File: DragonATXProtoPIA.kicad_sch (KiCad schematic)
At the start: 79 parts, among them IC1 MC6821, IC10 MT8816, IC11 74LS138, IC12 W65C51, IC13 MAX232, IC14 M48Tx2, IC15 74LS21, IC2 MC6821, IC3 74LS138, IC4 4050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

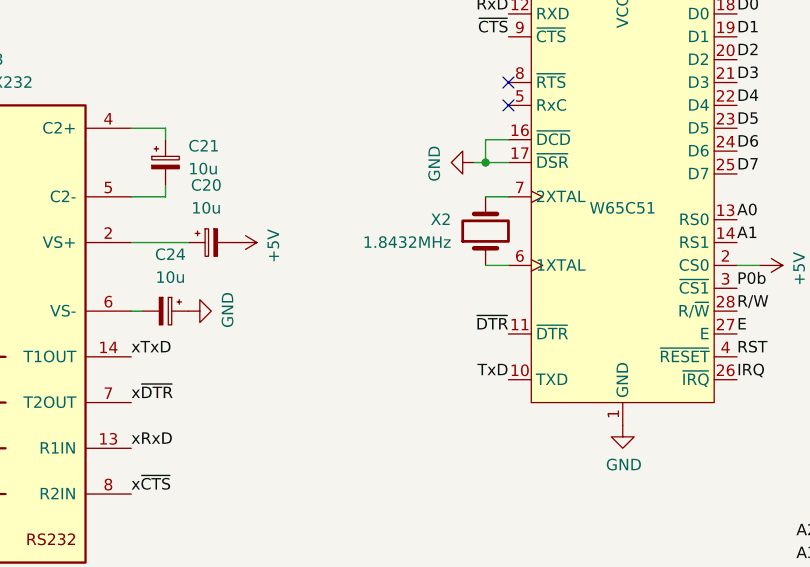
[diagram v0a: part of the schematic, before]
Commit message: Rectify slot edge and vertical dimensions
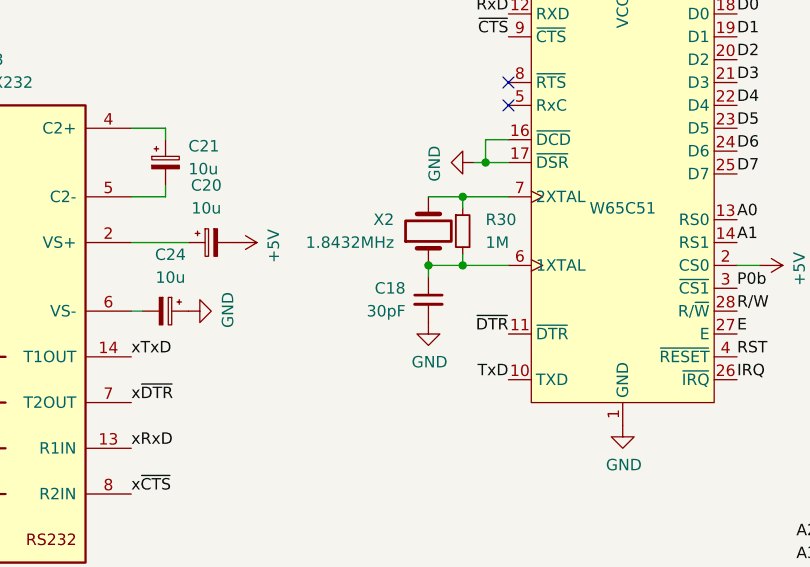
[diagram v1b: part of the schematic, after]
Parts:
- added C18: 30pF, Capacitor_THT:C_Disc_D4.3mm_W1.9mm_P5.00mm, symbol Device:C_Small
- added R30: 1M, Resistor_THT:R_Axial_DIN0204_L3.6mm_D1.6mm_P5.08mm_Horizontal, symbol Device:R_Small
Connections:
- net GND: now also C18.2
- net at IC12.6 (1XTAL), X2.1: now also C18.1, R30.2
- net at IC12.7 (2XTAL), X2.2: now also R30.1
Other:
- moved on the sheet: X2

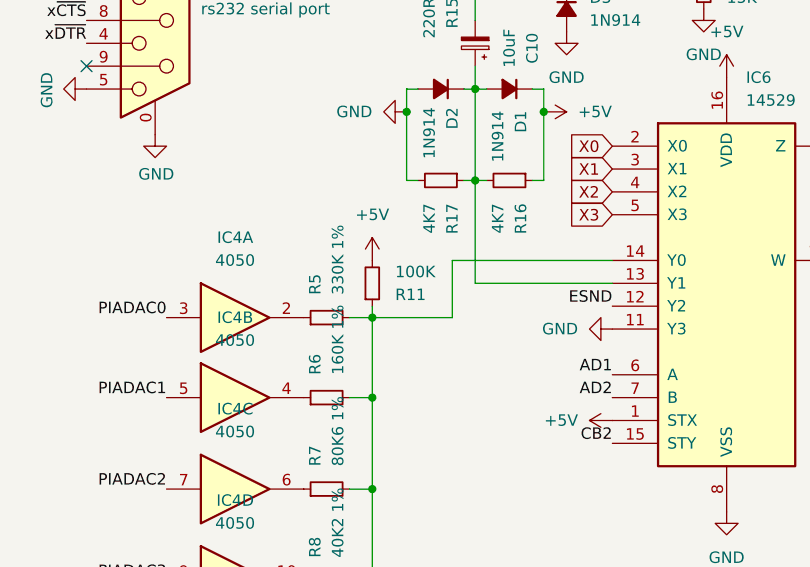
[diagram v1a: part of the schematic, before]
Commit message: shrink board
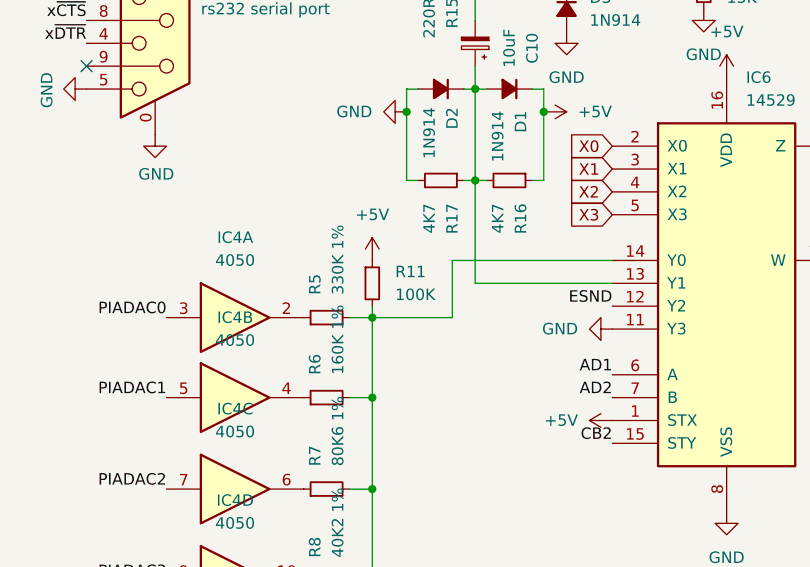
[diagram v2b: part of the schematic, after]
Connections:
- net +5V: now also R11.1; no longer R11.2
- net at C7.1, IC6.14 (Y0), IC7.6 (-)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: now also R11.2; no longer R11.1
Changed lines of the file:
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@@
 		(lib_id "Device:R_Small")
 		(at 238.76 213.36 0)
-		(mirror x)
 		(unit 1)
 		(exclude_from_sim no)
@@
 		(dnp no)
 		(property "Reference" "R11"
-			(at 241.3 214.6301 0)
+			(at 241.3 212.0899 0)
 			(effects
 				(font
@@
 		)
 		(property "Value" "100K"
-			(at 241.3 212.0901 0)
+			(at 241.3 214.6299 0)
 			(effects
 				(font

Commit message: remove uart and rtc
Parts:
- removed C16, C20, C21, C24: 10u, Capacitor_THT:CP_Radial_D6.3mm_P2.50mm, symbol Device:C_Polarized_Small
- removed C17: 100n, Capacitor_THT:C_Disc_D4.3mm_W1.9mm_P5.00mm, symbol Device:C_Small
- removed C18: 30pF, Capacitor_THT:C_Disc_D4.3mm_W1.9mm_P5.00mm, symbol Device:C_Small
- removed IC12: W65C51, Package_LCC:PLCC-28_THT-Socket, symbol Motorola PIA:6551
- removed IC13: MAX232, Package_DIP:DIP-16_W7.62mm, symbol Interface_UART:MAX232
- removed IC14: M48Tx2, Package_DIP:DIP-24_18.0mmx34.29mm_W15.24mm, symbol Memory_RAM:M48Tx2
- removed IC15: 74LS21, Package_DIP:DIP-14_W7.62mm, symbol 74xx:74LS21
- removed PL9: rs232 serial port, Connector_Dsub:DSUB-9_Socket_Horizontal_P2.77x2.84mm_EdgePinOffset9.90mm_Housed_MountingHolesOffset11.32mm, symbol Connector:DE9_Socket_MountingHoles
- removed R30: 1M, Resistor_THT:R_Axial_DIN0204_L3.6mm_D1.6mm_P5.08mm_Horizontal, symbol Device:R_Small
- removed X2: 1.8432MHz, Crystal:Crystal_HC18-U_Vertical, symbol Device:Crystal
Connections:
- net GND: now also IC8.1, IC8.2
- net R/W: no longer IC8.1, IC8.2
- no-connect marks 53 -> 47

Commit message: prepare for fabrication
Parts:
- PL1: now left out of the parts list
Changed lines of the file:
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@@
 		(unit 1)
 		(exclude_from_sim no)
-		(in_bom yes)
+		(in_bom no)
 		(on_board yes)
 		(dnp no)
@@
 		(unit 2)
 		(exclude_from_sim no)
-		(in_bom yes)
-		(on_board yes)
-		(dnp no)
+		(in_bom no)
+		(on_board yes)
+		(dnp no)
